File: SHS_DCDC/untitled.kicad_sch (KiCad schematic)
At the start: 0 parts

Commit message: ADC_PV & BAT
Blocks related to ADC reading of PV and BAT added on the physical board.
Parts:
- added C1, C35: 100nF, Capacitor_SMD:C_0402_1005Metric, symbol SHS_DCDC:C-Device
- added C30, C31: 10 uF, Capacitor_SMD:C_0805_2012Metric, symbol SHS_DCDC:C-Device
- added C32: 1 uF, Capacitor_SMD:C_0402_1005Metric, symbol SHS_DCDC:C-Device
- added C33, C34: 10 uF, Capacitor_SMD:C_0603_1608Metric, symbol Device:C
- added C4, C5: 22uF, Capacitor_SMD:C_0805_2012Metric, symbol SHS_DCDC:C-Device
- added J1: Barrel_Jack, digikey-footprints:Barrel_Jack_5.5mmODx2.1mmID_PJ-202A, symbol SHS_DCDC:Barrel_Jack-Connector
- added L1: NR8040T220M, Inductor_SMD:L_Taiyo-Yuden_NR-80xx, symbol SHS_DCDC:L-Device
- added Q1, Q15: BSS84, Package_TO_SOT_SMD:SOT-23, symbol SHS_DCDC:BSS84-Transistor_FET
- added Q14, Q16: PMV100XPEAR, digikey-kicad-library-master:SOT-23-3, symbol SHS_DCDC:PMV100XPEAR
- added R1: 100k, Resistor_SMD:R_0402_1005Metric, symbol SHS_DCDC:R-Device
- added R24, R3, R4: R, Resistor_SMD:R_0603_1608Metric, symbol SHS_DCDC:R-Device
- added R48, R7: 100k, Resistor_SMD:R_0603_1608Metric, symbol SHS_DCDC:R-Device
- added R6: 10k, Resistor_SMD:R_0603_1608Metric, symbol SHS_DCDC:R-Device
- added U1: RT8299-WDFN10L, Library:RT8299-WDFN, symbol SHS_DCDC:RT8299-WDFN10L
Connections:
- new net: C33.1, C34.1, Q1.1 (G), R6.2
- new net: Q1.3 (D), R24.2, R4.1
- new net: C1.1, U1.7 (BOOT)
- new net: C1.2, L1.2, U1.8 (SW)
- new net: Q1.2 (S), R3.2
- new net: R24.1, U1.1 (FB)
- new net: Q14.1 (G), Q15.2 (S), Q16.1 (G), R1.2
- new net: Q14.2 (S), Q16.2 (S)
- new net: C32.1, U1.4 (VCC)
- new net DCDC_OUT: C4.1, C5.1, L1.1, Q16.3 (D), R3.1
- new net GND: C30.2, C31.2, C32.2, C33.2, C34.2, C35.1, C4.2, C5.2, J1.2, Q15.3 (D), R4.2, R48.2, R7.1, U1.10 (GND)
- new net MCU_MPPT_ENABLE: C35.2, Q15.1 (G), R48.1, U1.3 (EN)
- new net MCU_PWM_MPPT: R6.1, R7.2
- new net PV: C30.1, C31.1, J1.1, Q14.3 (D), R1.1, U1.6 (VIN)
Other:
- note added: "Bidirectional switch"
- note added: "MCU_MPPT_ENABLE working principles: Sig 0 --> MPPT disabled, DCDC conv disabled, PV power flow through the bidirectional switch Sig 1 --> MPPT activated, DCDC conv enabled, bidirectional switch disabled, PV power flow through DCDC Sig is driven by the MCU. The MCU drives Sig if it is powered, otherwise Sig = 0 (pull down) Sig is activated by MCU when the Vbat is high enough (user setting)"

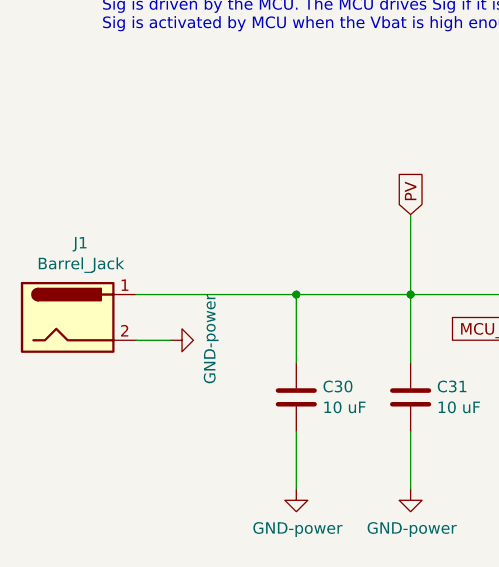
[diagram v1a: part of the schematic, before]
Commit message: 3D missing part
Many parts with no 3D view, have completed all of them
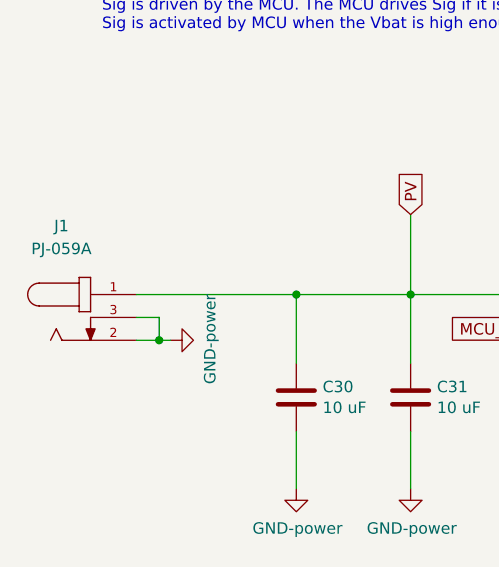
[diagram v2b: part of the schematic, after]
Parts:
- removed J1: Barrel_Jack, digikey-footprints:Barrel_Jack_5.5mmODx2.1mmID_PJ-202A, symbol SHS_DCDC:Barrel_Jack-Connector
- added J1: PJ-059A, SHS_DCDC:CUI_PJ-059A, symbol SHS_DCDC:PJ-059A
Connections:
- net GND: now also J1.2, J1.3
- net PV: now also J1.1
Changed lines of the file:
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@@
   (junction (at 95.25 87.63) (diameter 0) (color 0 0 0 0)
   )
+  (junction (at 39.37 88.9) (diameter 0) (color 0 0 0 0)
+  )
   (junction (at 200.66 101.6) (diameter 0) (color 0 0 0 0)
   )
@@
     (stroke (width 0) (type default) (color 0 0 0 0))
   )
+  (wire (pts (xy 39.37 86.36) (xy 39.37 88.9))
+    (stroke (width 0) (type default) (color 0 0 0 0))
+  )
   (wire (pts (xy 224.79 128.27) (xy 232.41 128.27))
     (stroke (width 0) (type default) (color 0 0 0 0))
@@
     (stroke (width 0) (type default) (color 0 0 0 0))
   )
+  (wire (pts (xy 36.83 86.36) (xy 39.37 86.36))
+    (stroke (width 0) (type default) (color 0 0 0 0))
+  )
   (wire (pts (xy 231.14 101.6) (xy 231.14 105.41))
     (stroke (width 0) (type default) (color 0 0 0 0))
@@
     (stroke (width 0) (type default) (color 0 0 0 0))
   )
+  (wire (pts (xy 39.37 88.9) (xy 40.64 88.9))
+    (stroke (width 0) (type default) (color 0 0 0 0))
+  )
   (wire (pts (xy 209.55 81.28) (xy 209.55 83.82))
     (stroke (width 0) (type default) (color 0 0 0 0))
@@
     (stroke (width 0) (type default) (color 0 0 0 0))
   )
-  (wire (pts (xy 36.83 88.9) (xy 40.64 88.9))
+  (wire (pts (xy 36.83 88.9) (xy 39.37 88.9))
     (stroke (width 0) (type default) (color 0 0 0 0))
   )
@@
     (pin "1")
   )
-  (symbol (lib_id "SHS_DCDC:Barrel_Jack-Connector") (at 29.21 86.36 0) (unit 1)
-    (in_bom yes) (on_board yes)
-    (property "Reference" "J1" (id 0) (at 30.6578 78.105 0))
-    (property "Value" "Barrel_Jack" (id 1) (at 30.6578 80.4164 0))
-    (property "Footprint" "digikey-footprints:Barrel_Jack_5.5mmODx2.1mmID_PJ-202A" (id 2) (at 30.48 87.376 0)
-      (effects (font (size 1.27 1.27)) hide)
-    )
-    (property "Datasheet" "~" (id 3) (at 30.48 87.376 0)
-      (effects (font (size 1.27 1.27)) hide)
-    )
-    (pin "1")
-    (pin "2")
+  (symbol (lib_id "SHS_DCDC:PJ-059A") (at 31.75 86.36 0) (unit 1)
+    (in_bom yes) (on_board yes) (fields_autoplaced)
+    (property "Reference" "J1" (id 0) (at 28.5115 76.2 0))
+    (property "Value" "PJ-059A" (id 1) (at 28.5115 78.74 0))
+    (property "Footprint" "SHS_DCDC:CUI_PJ-059A" (id 2) (at 31.75 78.74 0)
+      (effects (font (size 1.27 1.27)) (justify bottom) hide)
+    )
+    (property "Datasheet" "" (id 3) (at 31.75 86.36 0)
+      (effects (font (size 1.27 1.27)) hide)
+    )
+    (property "MANUFACTURER" "CUI INC" (id 4) (at 31.75 95.25 0)
+      (effects (font (size 1.27 1.27)) (justify bottom) hide)
+    )
+    (property "PARTREV" "1.02" (id 5) (at 31.75 96.52 0)
+      (effects (font (size 1.27 1.27)) (justify bottom) hide)
+    )
+    (property "STANDARD" "Manufacturer recommendations" (id 6) (at 31.75 76.2 0)
+      (effects (font (size 1.27 1.27)) (justify bottom) hide)
+    )
+    (pin "1")
+    (pin "2")
+    (pin "3")
   )
   (symbol (lib_id "SHS_DCDC:GND-power") (at 213.36 97.79 90) (unit 1)

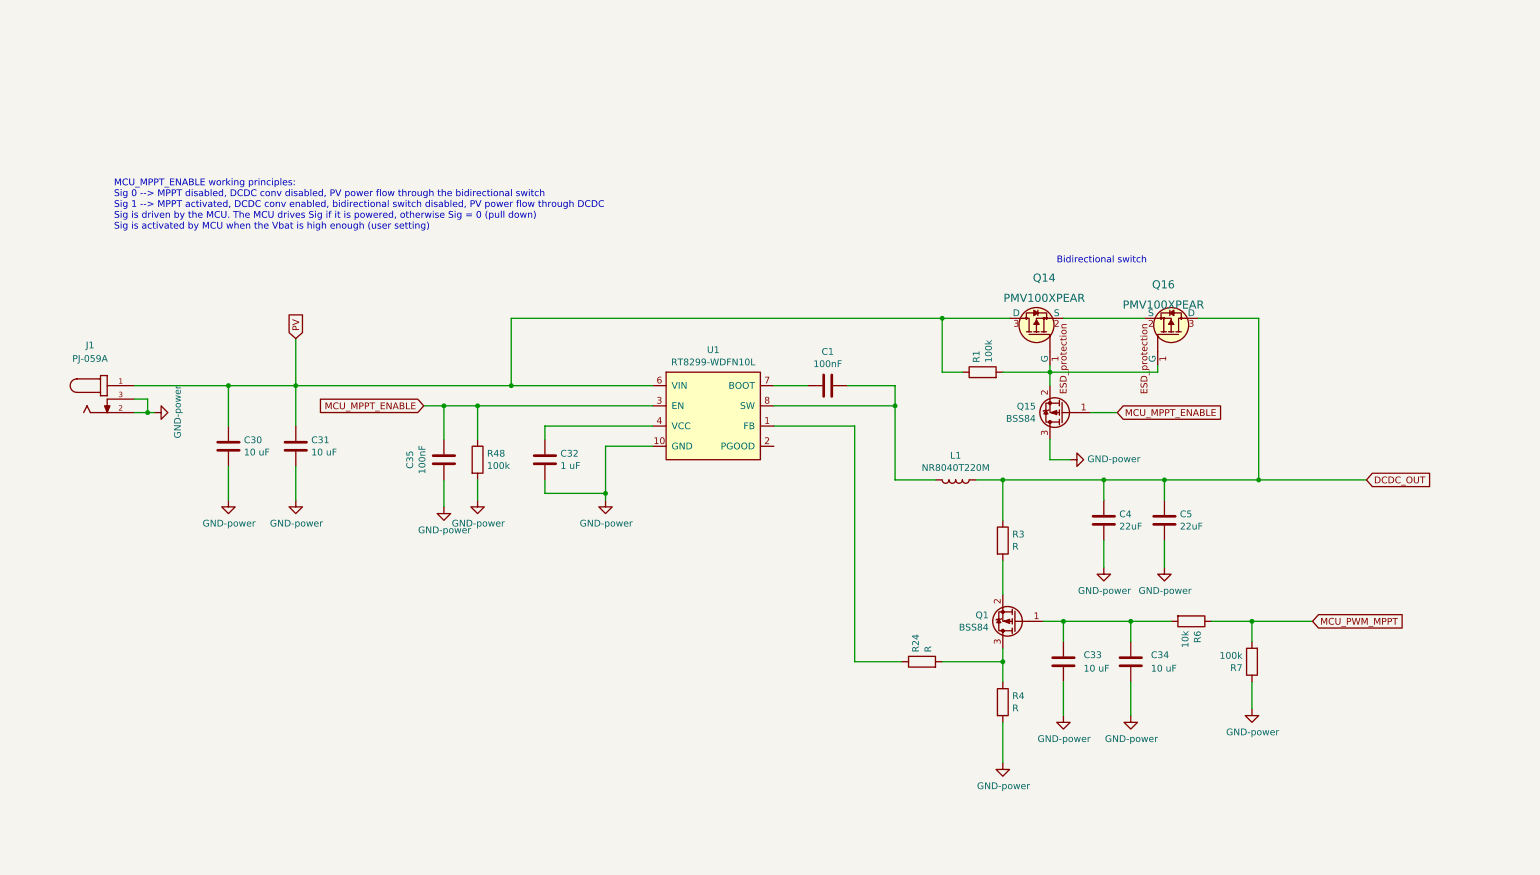
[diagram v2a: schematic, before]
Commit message: PV input Power
Big modification on the PV input power protection, precisely on the reverse battery current protection, and also on the switch between direct PV charging and the DCDC converter
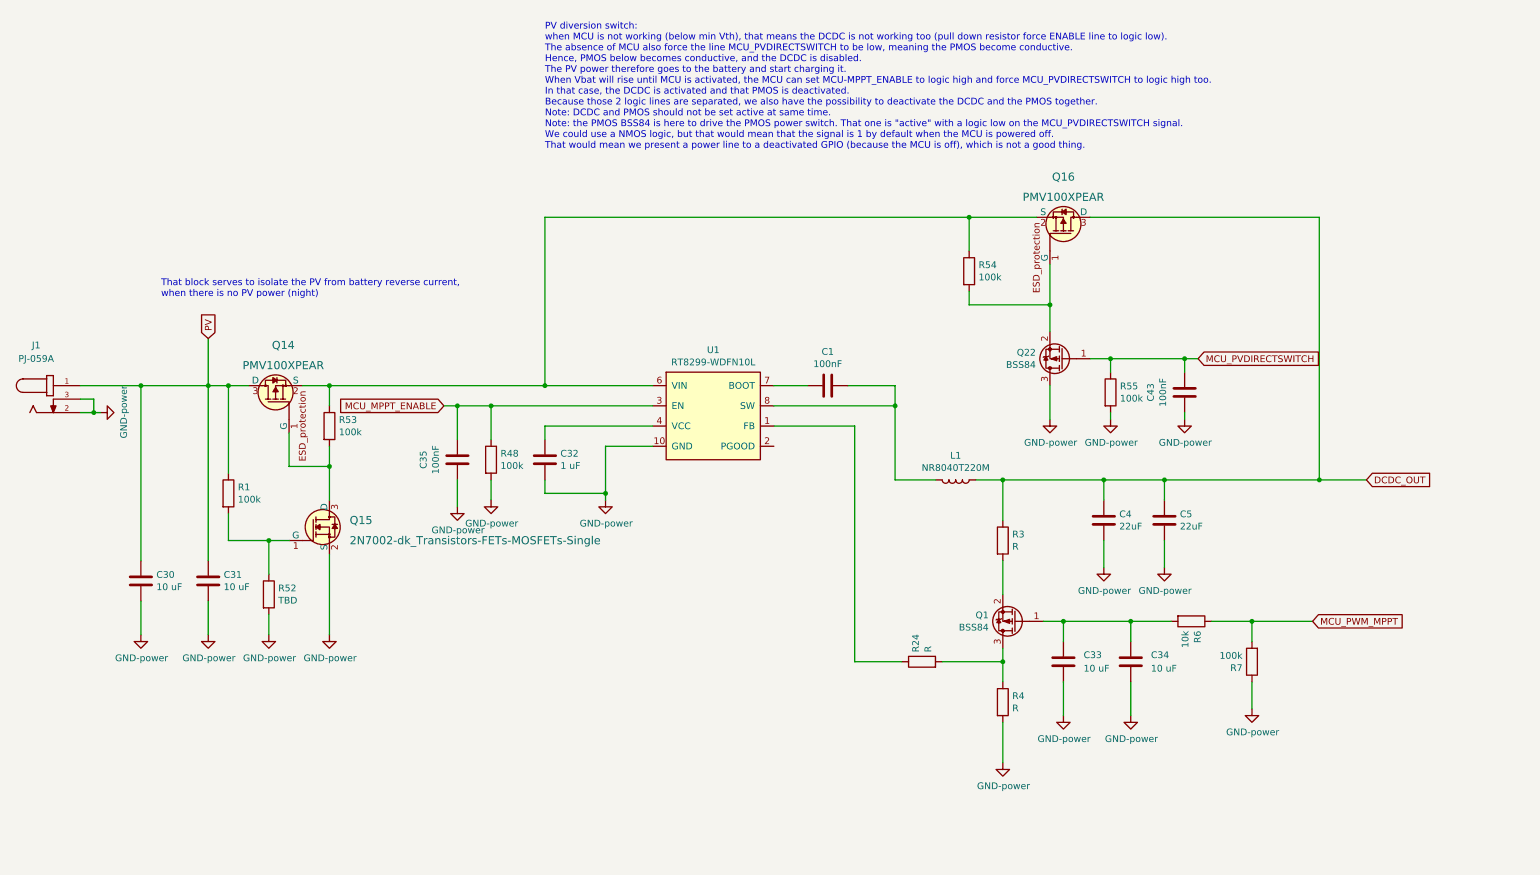
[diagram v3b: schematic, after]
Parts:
- removed Q15: BSS84, Package_TO_SOT_SMD:SOT-23, symbol SHS_DCDC:BSS84-Transistor_FET
- added C43: 100nF, Capacitor_SMD:C_0402_1005Metric, symbol SHS_DCDC:C-Device
- added Q15: 2N7002-dk_Transistors-FETs-MOSFETs-Single, digikey-footprints:SOT-23-3, symbol SHS_DCDC:2N7002-dk_Transistors-FETs-MOSFETs-Single
- added Q22: BSS84, Package_TO_SOT_SMD:SOT-23, symbol SHS_DCDC:BSS84-Transistor_FET
- added R52: TBD, Resistor_SMD:R_0402_1005Metric, symbol SHS_DCDC:R-Device
- added R53, R54, R55: 100k, Resistor_SMD:R_0402_1005Metric, symbol SHS_DCDC:R-Device
- R24, R3, R4, R48, R6, R7: footprint Resistor_SMD:R_0603_1608Metric -> Resistor_SMD:R_0402_1005Metric
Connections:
- net GND: now also C43.1, Q15.2 (S), Q22.3 (D), R52.2, R55.2
- net PV: no longer U1.6 (VIN)
- net at Q14.2 (S), Q16.2 (S): now also U1.6 (VIN), R53.1, R54.1
- new net: Q16.1 (G), Q22.2 (S), R54.2
- new net: Q15.1 (G), R1.2, R52.1
- new net: Q14.1 (G), Q15.3 (D), R53.2
- new net MCU_PVDIRECTSWITCH: C43.2, Q22.1 (G), R55.1
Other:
- note added: "PV diversion switch: when MCU is not working (below min Vth), that means the DCDC is not working too (pull down resistor force ENABLE line to logic low). The absence of MCU also force the line MCU_PVDIRECTSWITCH to be low, meaning the PMOS become conductive. Hence, PMOS below becomes conductive, and the DCDC is disabled. The PV power therefore goes to the battery and start charging it. When Vbat 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"
- note added: "That block serves to isolate the PV from battery reverse current, when there is no PV power (night)"
- note removed: "Bidirectional switch"
- note removed: "MCU_MPPT_ENABLE working principles: Sig 0 --> MPPT disabled, DCDC conv disabled, PV power flow through the bidirectional switch Sig 1 --> MPPT activated, DCDC conv enabled, bidirectional switch disabled, PV power flow through DCDC Sig is driven by the MCU. The MCU drives Sig if it is powered, otherwise Sig = 0 (pull down) Sig is activated by MCU when the Vbat is high enough (user setting)"
- moved on the sheet: C30, C31, C35, J1, Q14, Q16, R48

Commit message: Final_check stage
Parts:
- removed Q22: BSS84, Package_TO_SOT_SMD:SOT-23, symbol SHS_DCDC:BSS84-Transistor_FET
- added D1: 1N4148, Diode_SMD:D_SOD-123, symbol Diode:1N4148
- added Q22, Q23: 2N7002-dk_Transistors-FETs-MOSFETs-Single, digikey-footprints:SOT-23-3, symbol SHS_DCDC:2N7002-dk_Transistors-FETs-MOSFETs-Single
- added R64: 100k, Resistor_SMD:R_0402_1005Metric, symbol SHS_DCDC:R-Device
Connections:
- net GND: now also Q22.2 (S), Q23.2 (S)
- net MCU_PVDIRECTSWITCH: now also Q22.1 (G)
- net at C1.1, U1.7 (BOOT): now also D1.1 (K)
- net at Q14.2 (S), Q16.2 (S), R53.1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: now also R64.2
- net at Q16.1 (G): now also Q23.3 (D), R64.1; no longer R54.2
- new net: Q22.3 (D), Q23.1 (G), R54.2
- new net 5V: D1.2 (A)
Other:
- note added: "PV diversion switch: when MCU is not working (below min Vth), that means the DCDC is not working too (pull down resistor force ENABLE line to logic low). The absence of MCU also forces the line MCU_PVDIRECTSWITCH to be low, meaning the PMOS become conductive. Hence, PMOS below becomes conductive, and the DCDC is disabled. The PV power therefore flows into the battery and start charging it. When V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"
- note added: "Vinput < 5V5 The diode boostrap is recommended See datasheet"
- note removed: "PV diversion switch: when MCU is not working (below min Vth), that means the DCDC is not working too (pull down resistor force ENABLE line to logic low). The absence of MCU also force the line MCU_PVDIRECTSWITCH to be low, meaning the PMOS become conductive. Hence, PMOS below becomes conductive, and the DCDC is disabled. The PV power therefore goes to the battery and start charging it. When Vbat 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"
- moved on the sheet: C43, Q16, R54, R55
